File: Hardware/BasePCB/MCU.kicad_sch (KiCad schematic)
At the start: 12 parts, among them J7 Conn_01x04, Q10 IRLML0030, Q11 IRLML0030, U5 LeaderSOM

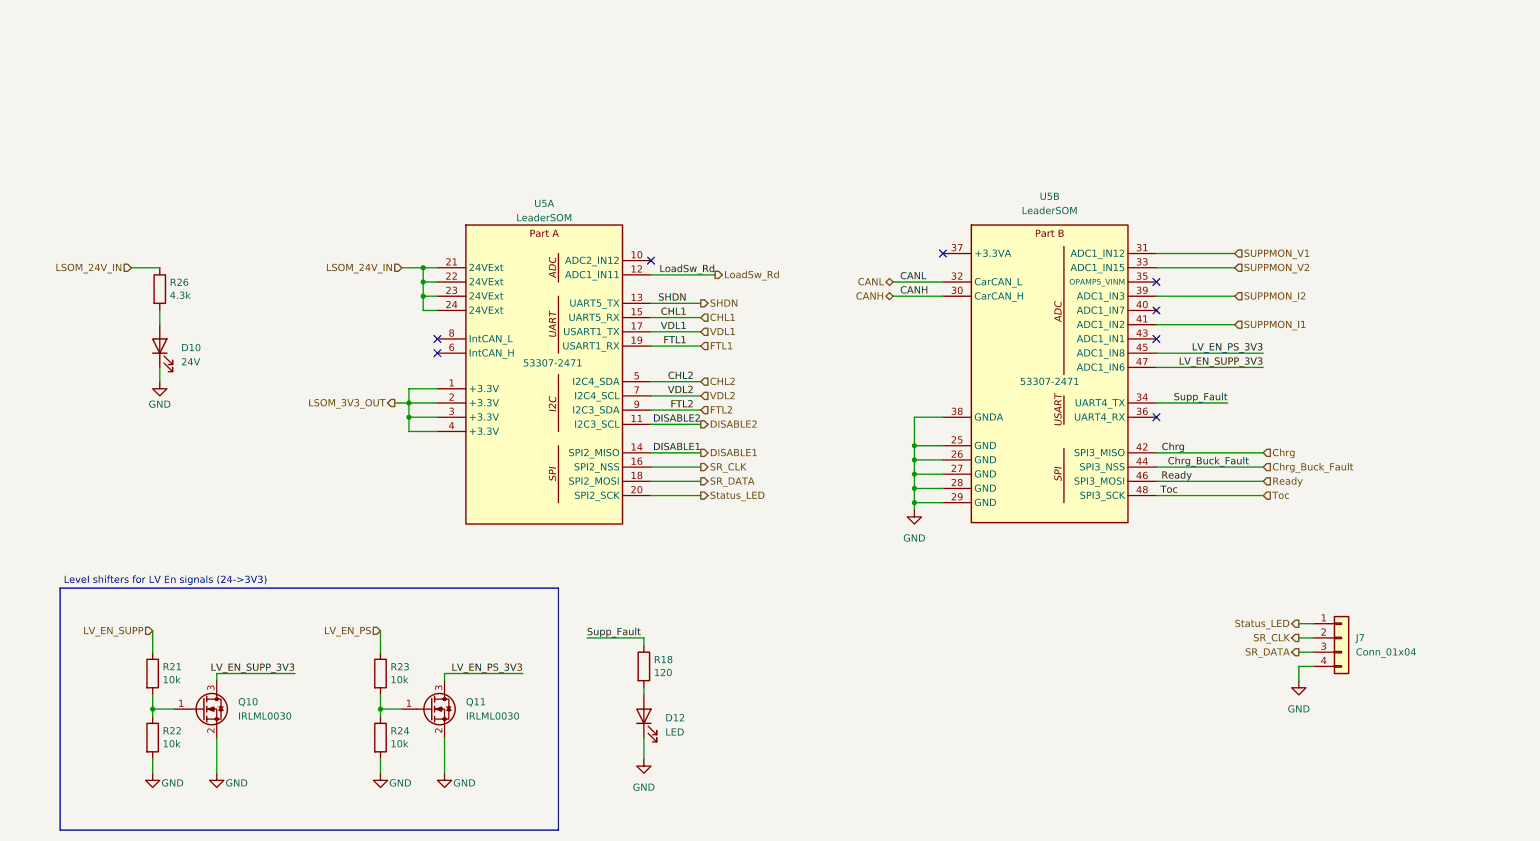
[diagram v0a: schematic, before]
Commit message: add LPF to ADC inputs
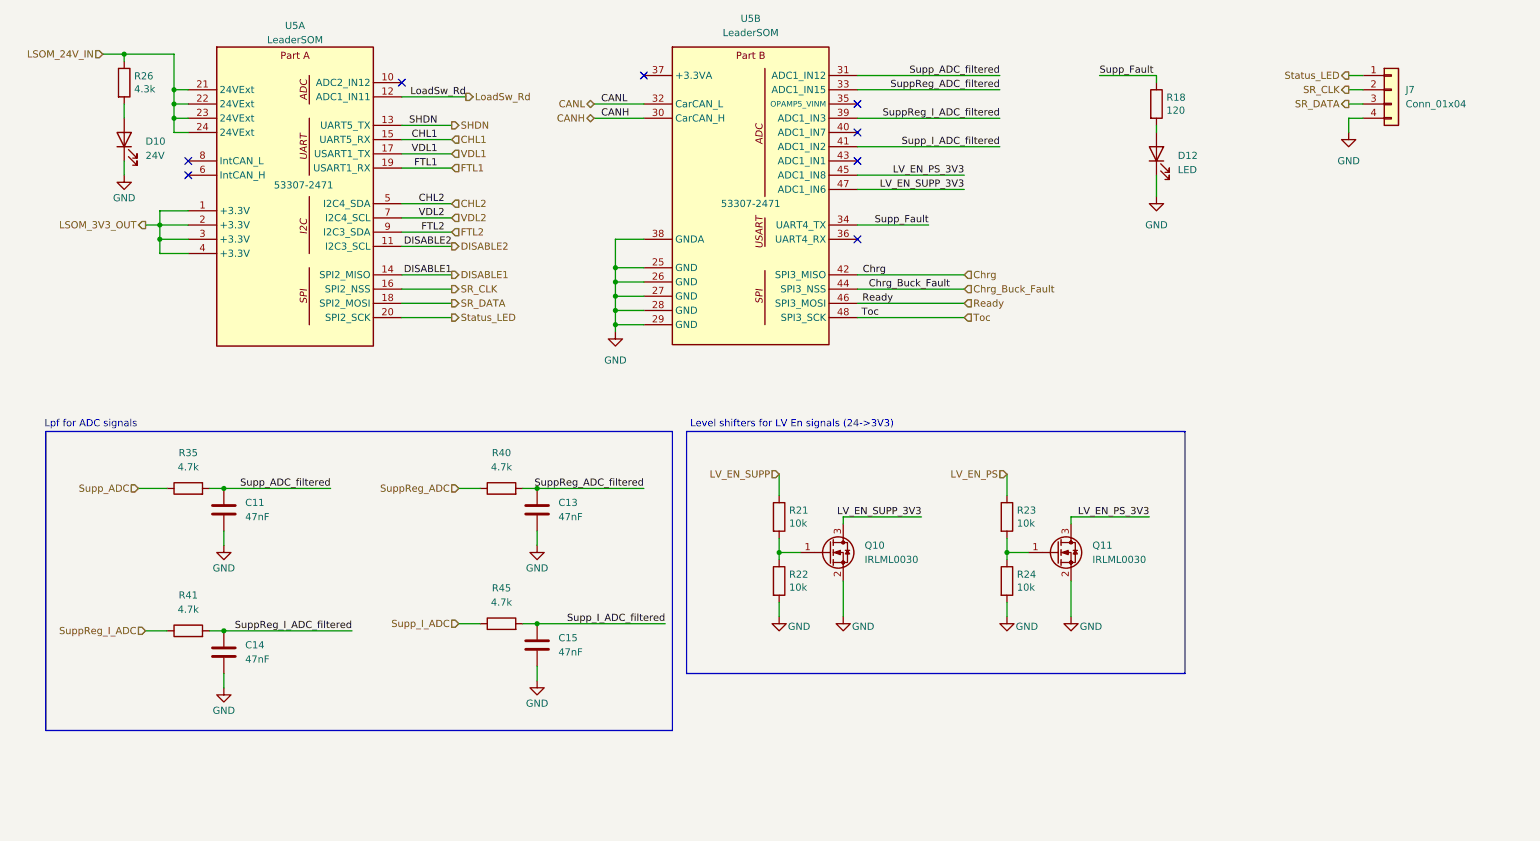
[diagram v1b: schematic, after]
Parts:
- added C11, C13, C14, C15: 47nF, Capacitor_SMD:C_0603_1608Metric_Pad1.08x0.95mm_HandSolder, symbol Device:C
- added R35, R40, R41, R45: 4.7k, Resistor_SMD:R_0603_1608Metric_Pad0.98x0.95mm_HandSolder, symbol Device:R
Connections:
- net GND: now also C11.2, C13.2, C14.2, C15.2
- net SUPPMON_I1 renamed Supp_I_ADC_filtered
- net Supp_I_ADC_filtered: now also C15.1, R45.2
- net SUPPMON_I2 renamed SuppReg_I_ADC_filtered
- net SuppReg_I_ADC_filtered: now also C14.1, R41.2
- net SUPPMON_V1 renamed Supp_ADC_filtered
- net Supp_ADC_filtered: now also C11.1, R35.2
- net SUPPMON_V2 renamed SuppReg_ADC_filtered
- net SuppReg_ADC_filtered: now also C13.1, R40.2
- new net SuppReg_ADC: R40.1
- new net SuppReg_I_ADC: R41.1
- new net Supp_ADC: R35.1
- new net Supp_I_ADC: R45.1
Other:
- note added: "Lpf for ADC signals"
- moved on the sheet: D10, D12, J7, Q10, Q11, R18, R21, R22, R23, R24, R26, U5A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

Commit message: schem done?
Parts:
- added R7, R8: 10k, Resistor_SMD:R_0603_1608Metric_Pad0.98x0.95mm_HandSolder, symbol Device:R
- renumbered R41 to R9
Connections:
- net LoadSw_Rd is gone; now on net VDL2: U5.12 (ADC1_IN11)
- net CHL2: now also U5.10 (ADC2_IN12); no longer U5.5 (I2C4_SDA)
- net LSOM_3V3_OUT: now also R7.1, R8.1
- net VDL2: no longer U5.7 (I2C4_SCL)
- net Chrg renamed SuppCharger_En
- net Chrg_Buck_Fault renamed SuppCharger_Stat1
- net Ready renamed SuppCharger_Stat2
- net Toc renamed SuppCharger_~{INT}
- new net I2C_SCL: R7.2, U5.7 (I2C4_SCL)
- new net I2C_SDA: R8.2, U5.5 (I2C4_SDA)
- no-connect marks 8 -> 7

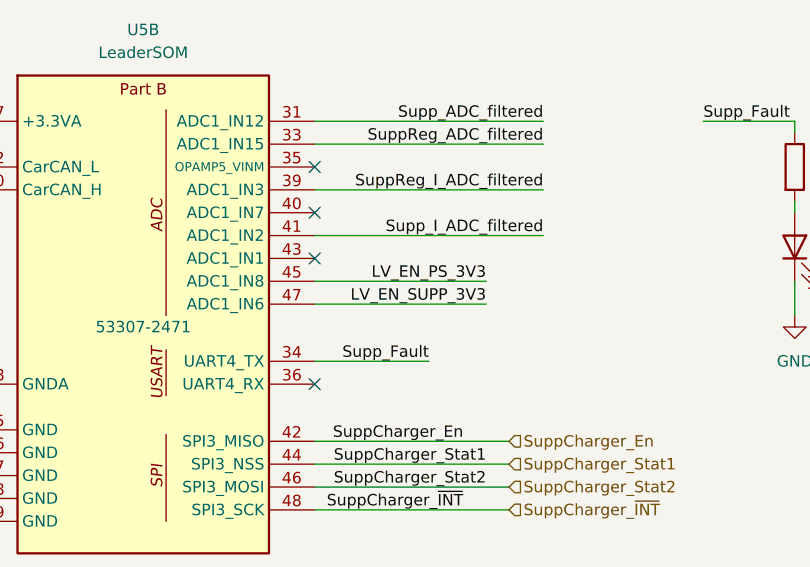
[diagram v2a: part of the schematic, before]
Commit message: supp charger routing done
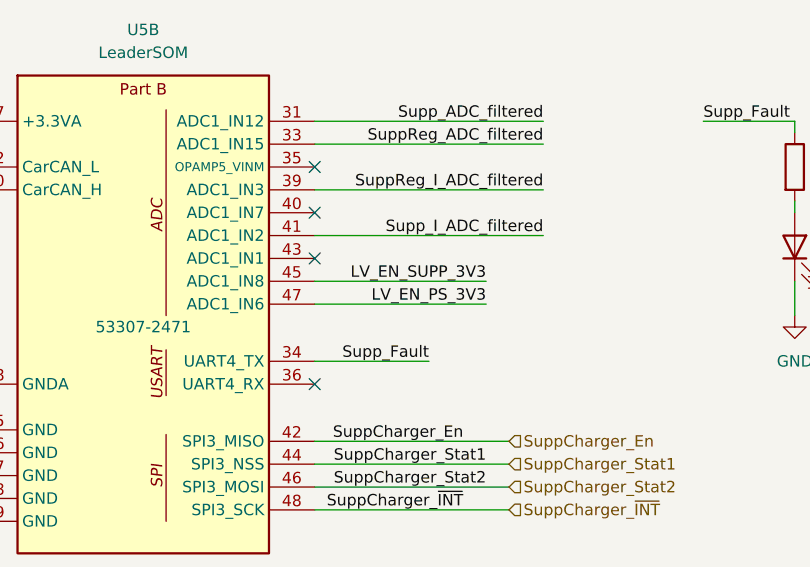
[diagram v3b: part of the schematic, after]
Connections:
- net LV_EN_PS_3V3: now also U5.47 (ADC1_IN6); no longer U5.45 (ADC1_IN8)
- net LV_EN_SUPP_3V3: now also U5.45 (ADC1_IN8); no longer U5.47 (ADC1_IN6)
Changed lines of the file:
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@@
 	(wire
 		(pts
+			(xy 165.1 50.8) (xy 184.15 50.8)
+		)
+		(stroke
+			(width 0)
+			(type default)
+		)
+	)
+	(wire
+		(pts
 			(xy 260.35 68.58) (xy 259.08 69.85)
 		)
@@
 	(wire
 		(pts
-			(xy 165.1 48.26) (xy 184.15 48.26)
-		)
-		(stroke
-			(width 0)
-			(type default)
-		)
-	)
-	(wire
-		(pts
 			(xy 43.18 33.02) (xy 43.18 35.56)
 		)
@@
 	(wire
 		(pts
-			(xy 165.1 50.8) (xy 184.15 50.8)
+			(xy 121.92 69.85) (xy 127 69.85)
 		)
 		(stroke
@@
 	(wire
 		(pts
-			(xy 121.92 69.85) (xy 127 69.85)
+			(xy 191.77 115.57) (xy 191.77 116.84)
 		)
 		(stroke
@@
 	(wire
 		(pts
-			(xy 191.77 115.57) (xy 191.77 116.84)
+			(xy 151.13 113.03) (xy 151.13 115.57)
 		)
 		(stroke
@@
 	(wire
 		(pts
-			(xy 151.13 113.03) (xy 151.13 115.57)
+			(xy 49.53 129.54) (xy 52.07 129.54)
 		)
 		(stroke
@@
 	(wire
 		(pts
-			(xy 49.53 129.54) (xy 52.07 129.54)
+			(xy 127 64.77) (xy 121.92 64.77)
 		)
 		(stroke
@@
 	(wire
 		(pts
-			(xy 127 64.77) (xy 121.92 64.77)
+			(xy 83.82 46.99) (xy 92.71 46.99)
 		)
 		(stroke
@@
 	(wire
 		(pts
-			(xy 83.82 46.99) (xy 92.71 46.99)
+			(xy 165.1 48.26) (xy 184.15 48.26)
 		)
 		(stroke
@@
 	)
 	(label "LV_EN_PS_3V3"
-		(at 184.15 48.26 180)
+		(at 184.15 50.8 180)
 		(effects
 			(font
@@
 	)
 	(label "LV_EN_SUPP_3V3"
-		(at 184.15 50.8 180)
+		(at 184.15 48.26 180)
 		(effects
 			(font

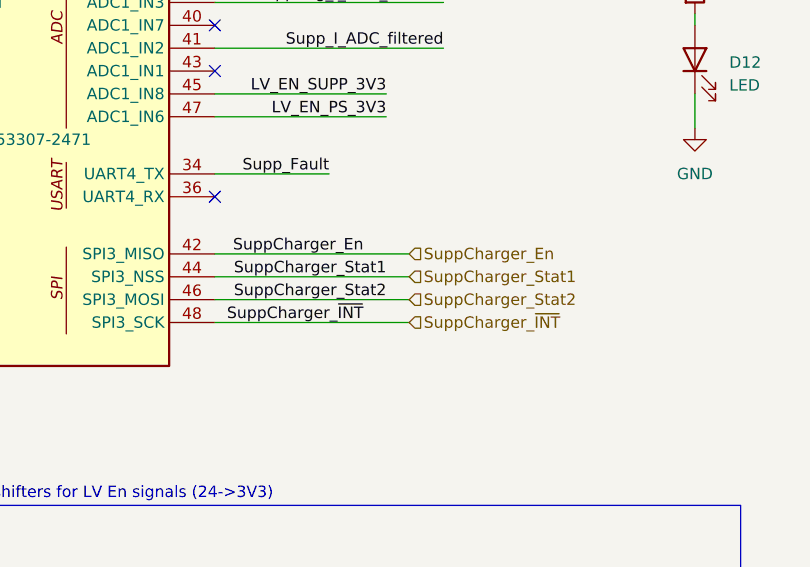
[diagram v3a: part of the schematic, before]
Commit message: swap stat pins in supp charger
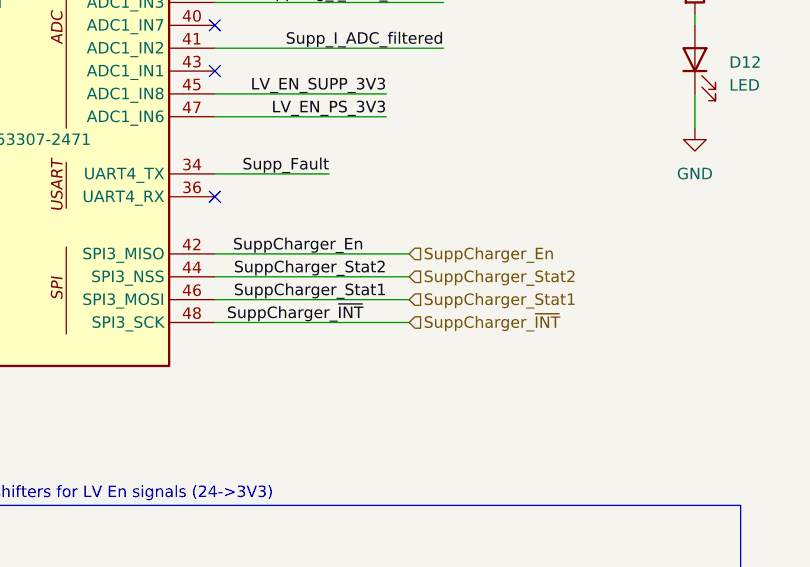
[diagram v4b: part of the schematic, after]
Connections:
- net SuppCharger_Stat1: now also U5.46 (SPI3_MOSI); no longer U5.44 (SPI3_NSS)
- net SuppCharger_Stat2: now also U5.44 (SPI3_NSS); no longer U5.46 (SPI3_MOSI)
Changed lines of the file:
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@@
 	(wire
 		(pts
-			(xy 165.1 68.58) (xy 186.69 68.58)
-		)
-		(stroke
-			(width 0)
-			(type default)
-		)
-	)
-	(wire
-		(pts
 			(xy 43.18 38.1) (xy 43.18 40.64)
 		)
@@
 	(wire
 		(pts
-			(xy 165.1 71.12) (xy 186.69 71.12)
-		)
-		(stroke
-			(width 0)
-			(type default)
-		)
-	)
-	(wire
-		(pts
 			(xy 83.82 53.34) (xy 96.52 53.34)
 		)
@@
 	(wire
 		(pts
+			(xy 165.1 71.12) (xy 186.69 71.12)
+		)
+		(stroke
+			(width 0)
+			(type default)
+		)
+	)
+	(wire
+		(pts
 			(xy 242.57 69.85) (xy 259.08 69.85)
 		)
@@
 	(wire
 		(pts
+			(xy 165.1 68.58) (xy 186.69 68.58)
+		)
+		(stroke
+			(width 0)
+			(type default)
+		)
+	)
+	(wire
+		(pts
 			(xy 248.92 58.42) (xy 252.73 58.42)
 		)
@@
 	)
 	(label "SuppCharger_Stat2"
-		(at 184.15 71.12 180)
+		(at 184.15 68.58 180)
 		(effects
 			(font
@@
 	)
 	(label "SuppCharger_Stat1"
-		(at 184.15 68.58 180)
+		(at 184.15 71.12 180)
 		(effects
 			(font
@@
 	(hierarchical_label "SuppCharger_Stat1"
 		(shape input)
-		(at 186.69 68.58 0)
+		(at 186.69 71.12 0)
 		(effects
 			(font
@@
 	(hierarchical_label "SuppCharger_Stat2"
 		(shape input)
-		(at 186.69 71.12 0)
+		(at 186.69 68.58 0)
 		(effects
 			(font

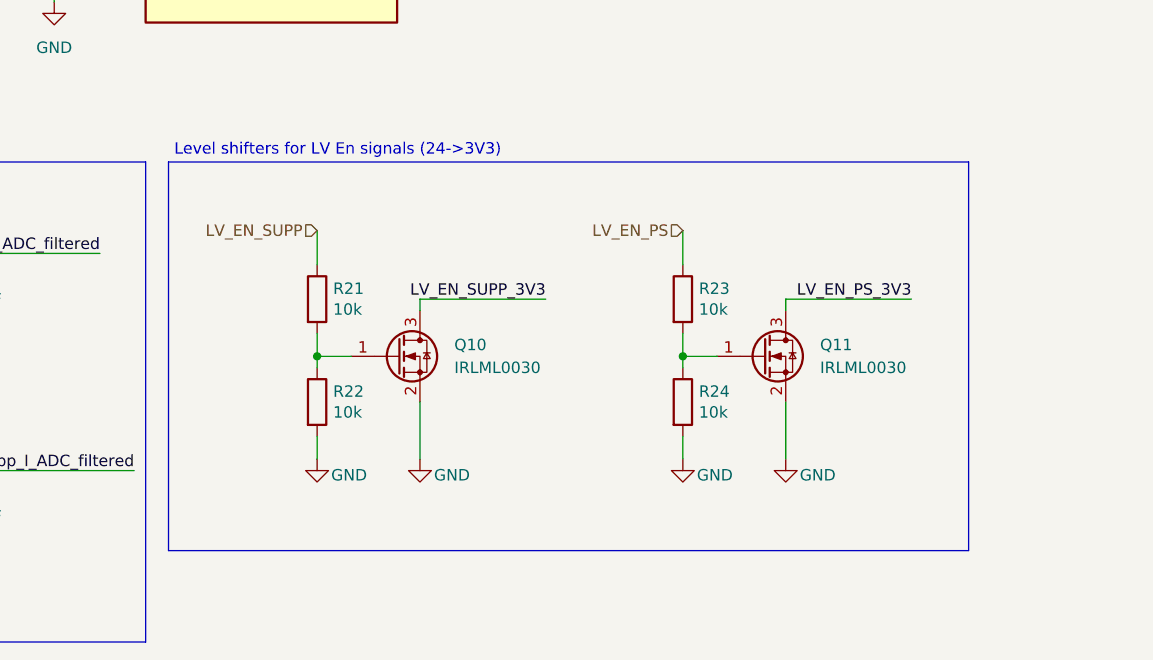
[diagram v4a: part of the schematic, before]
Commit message: supp bat hall effect routing
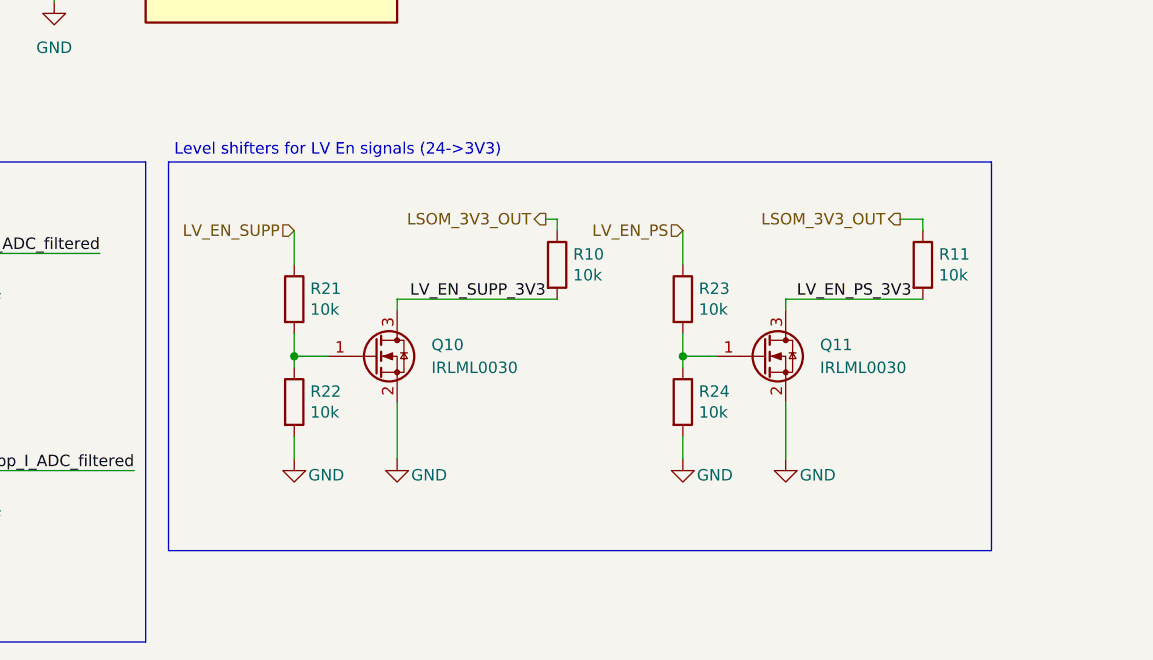
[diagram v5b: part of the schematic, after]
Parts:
- added R10, R11: 10k, Resistor_SMD:R_0603_1608Metric_Pad0.98x0.95mm_HandSolder, symbol Device:R
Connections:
- net LSOM_3V3_OUT: now also R10.1, R11.1
- net LV_EN_PS_3V3: now also R11.2
- net LV_EN_SUPP_3V3: now also R10.2
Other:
- moved on the sheet: Q10, R21, R22
